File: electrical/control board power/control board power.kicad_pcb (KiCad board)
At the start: 2 copper layers, 147.3 x 147.3 mm, 80 parts, among them J1 Conn_01x02, J10 48V_from_conversion, J17 Switch_B, J18 Switch_C, J19 Switch_D, J2 5V, J3 Barrel_Jack, J4 Switch_A, J5 Switch_Input, J6 Power_Connector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

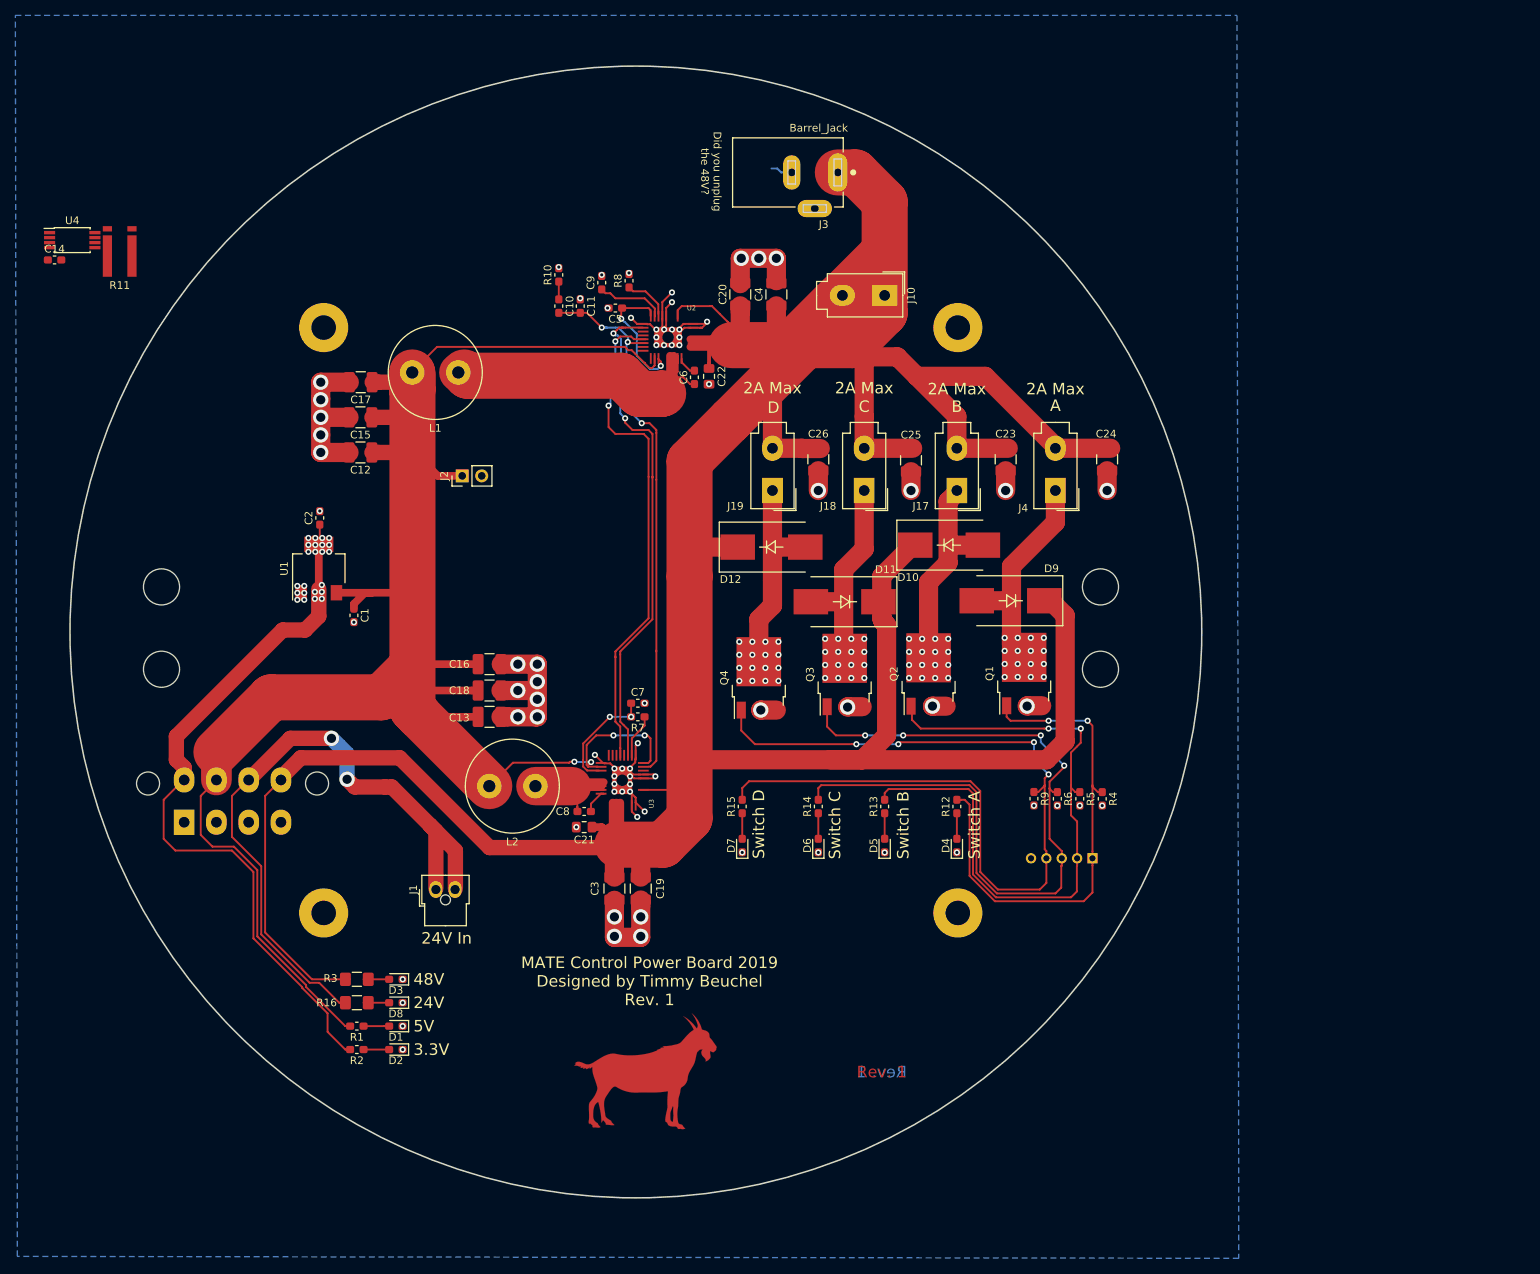
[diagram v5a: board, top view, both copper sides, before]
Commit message: Switched location of low side switches
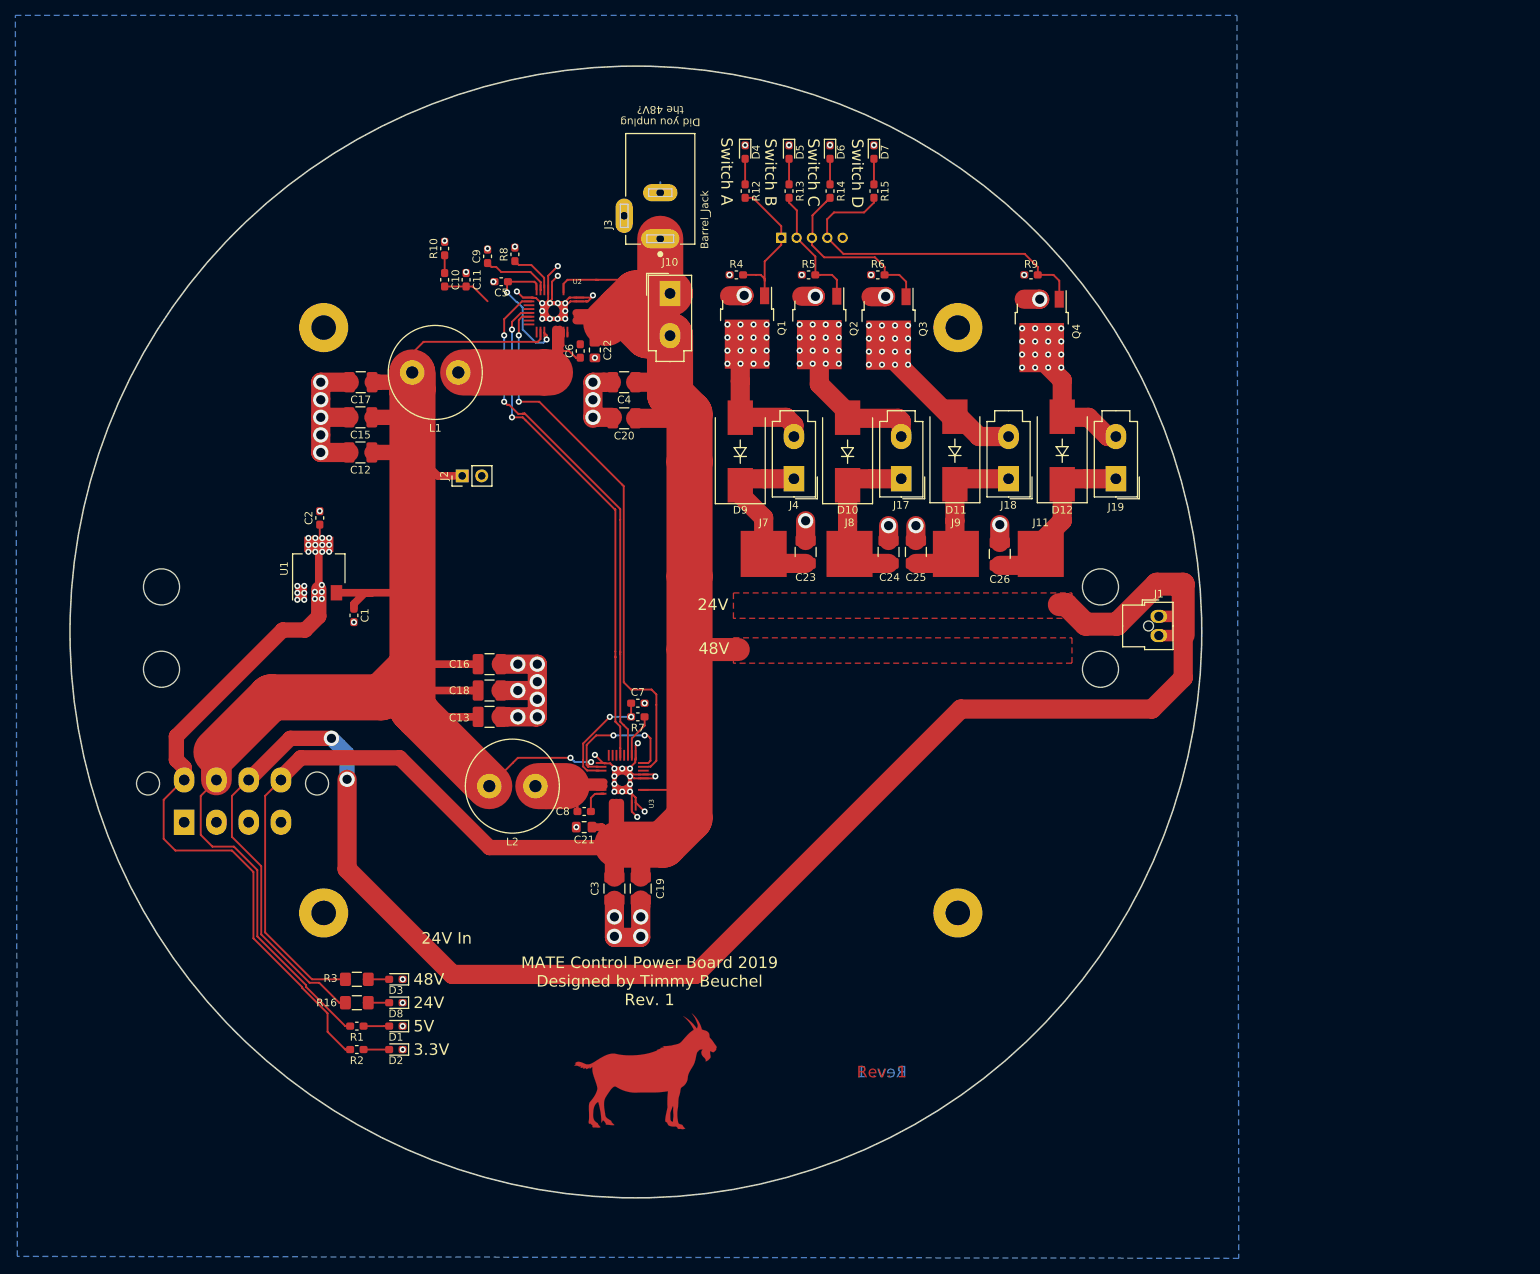
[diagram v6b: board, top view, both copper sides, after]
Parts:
- removed C14: C_Small, Capacitor_SMD:C_0603_1608Metric_Pad1.05x0.95mm_HandSolder
- removed R11: 1m, footprints:FC4L64
- removed U4: INA240-INA240, Package_SO:TSSOP-8_4.4x3mm_P0.65mm
- added J11: Switch_D_High, footprints:Square_Pad_6mm, F.Cu at (154.3, 87.6)
- added J7: Switch_A_High, footprints:Square_Pad_6mm, F.Cu at (118.2, 87.6)
- added J8: Switch_B_High, footprints:Square_Pad_6mm, F.Cu at (129.4, 87.6)
- added J9: Switch_C_High, footprints:Square_Pad_6mm, F.Cu at (143.3, 87.6)
- moved J1 100.6 mm to (169.7, 100.3), turned to 0 degrees
- moved D4 94.4 mm to (115.8, 39.9), turned to 270 degrees
- moved D7 91.9 mm to (132.6, 39.9), turned to 270 degrees
- moved D5 91.1 mm to (121.5, 39.9), turned to 270 degrees
- moved J5 90.4 mm to (120.5, 51.1), turned to 0 degrees
- moved D6 90.3 mm to (126.9, 39.9), turned to 270 degrees
- moved R12 84.7 mm to (115.8, 45.0), turned to 270 degrees
- moved R4 83.2 mm to (114.7, 55.9), turned to 180 degrees
- moved R15 81.9 mm to (132.6, 45.0), turned to 270 degrees
- moved R13 81.1 mm to (121.5, 45.0), turned to 270 degrees
- moved R14 80.1 mm to (126.9, 45.0), turned to 270 degrees
- moved R5 76.8 mm to (124.1, 55.9), turned to 180 degrees
- moved R6 72.1 mm to (133.1, 55.9), turned to 180 degrees
- moved R9 68.2 mm to (153.0, 55.9), turned to 180 degrees
- moved Q4 58.2 mm to (154.4, 63.2), turned to 270 degrees
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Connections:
- C23 pad 2: +48V -> /SWITCH_A_HIGH
- C24 pad 2: +48V -> /SWITCH_B_HIGH
- C25 pad 2: +48V -> /SWITCH_C_HIGH
- C26 pad 2: +48V -> /SWITCH_D_HIGH
- D10 pad 1: +48V -> /SWITCH_B_HIGH
- D11 pad 1: +48V -> /SWITCH_C_HIGH
- D12 pad 1: +48V -> /SWITCH_D_HIGH
- D9 pad 1: +48V -> /SWITCH_A_HIGH
- J17 pad 1: Net-(D10-Pad2) -> /SWITCH_B_HIGH
- J17 pad 2: +48V -> Net-(D10-Pad2)
- J18 pad 1: Net-(D11-Pad2) -> /SWITCH_C_HIGH
- J18 pad 2: +48V -> Net-(D11-Pad2)
- J19 pad 1: Net-(D12-Pad2) -> /SWITCH_D_HIGH
- J19 pad 2: +48V -> Net-(D12-Pad2)
- J4 pad 1: Net-(D9-Pad2) -> /SWITCH_A_HIGH
- J4 pad 2: +48V -> Net-(D9-Pad2)
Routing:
- net +48V: track 474.1 -> 240.0 mm
- net +24V: track 88.5 -> 236.9 mm
- net /SWITCH_C: track 100.0 -> 24.0 mm, vias 4 -> 0
- net /SWITCH_D: track 116.8 -> 45.6 mm, vias 4 -> 0
- net /SWITCH_B: track 86.8 -> 16.4 mm, vias 2 -> 0
- net /SWITCH_A: track 64.9 -> 19.3 mm, vias 2 -> 0
- net /SWITCH_D_HIGH: track 0.00 -> 19.6 mm
- net /SWITCH_A_HIGH: track 0.00 -> 19.6 mm
- net /SWITCH_C_HIGH: track 0.00 -> 18.6 mm
- net /SWITCH_B_HIGH: track 0.00 -> 18.3 mm
- net +5V: track 258.0 -> 241.5 mm
- net Net-(C6-Pad2): track 39.8 -> 23.3 mm
- net Net-(D12-Pad2): track 27.1 -> 15.9 mm
- net Net-(D9-Pad2): track 28.6 -> 18.8 mm
- net Net-(D10-Pad2): track 27.5 -> 19.9 mm
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- added copper zone on F.Cu, net +24V
- added copper zone on F.Cu, net +48V
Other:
- board text removed: "2A Max"
- board text removed: "A"
- board text removed: "B"
- board text removed: "C"
- board text removed: "D"

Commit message: added diode marks to diodes
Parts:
- D1, D2, D3, D4, D5, D6, D7, D8: footprint LED_SMD:LED_0603_1608Metric_Pad1.05x0.95mm_HandSolder -> footprints:LED_0603_1608Metric_Pad1.05x0.95mm_HandSolder_diode_mark
- moved R10 6.73 mm to (76.6, 59.2), turned to 180 degrees
- moved R8 5.69 mm to (91.1, 55.5), turned to 0 degrees
- moved C9 5.59 mm to (87.5, 55.5), turned to 180 degrees
- moved C10 4.60 mm to (79.6, 60.1)
- moved C11 4.60 mm to (82.4, 60.1)
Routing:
- net Net-(C9-Pad1): track 8.99 -> 3.13 mm
- net Net-(R8-Pad1): track 5.98 -> 2.25 mm
- net Net-(C6-Pad1): track 0.46 -> 3.29 mm
- net +24V: track 236.9 -> 238.9 mm
- net GND: track 127.2 -> 125.2 mm, vias 84 -> 83
- net Net-(C10-Pad2): track 77.5 -> 79.2 mm, vias 2 -> 3

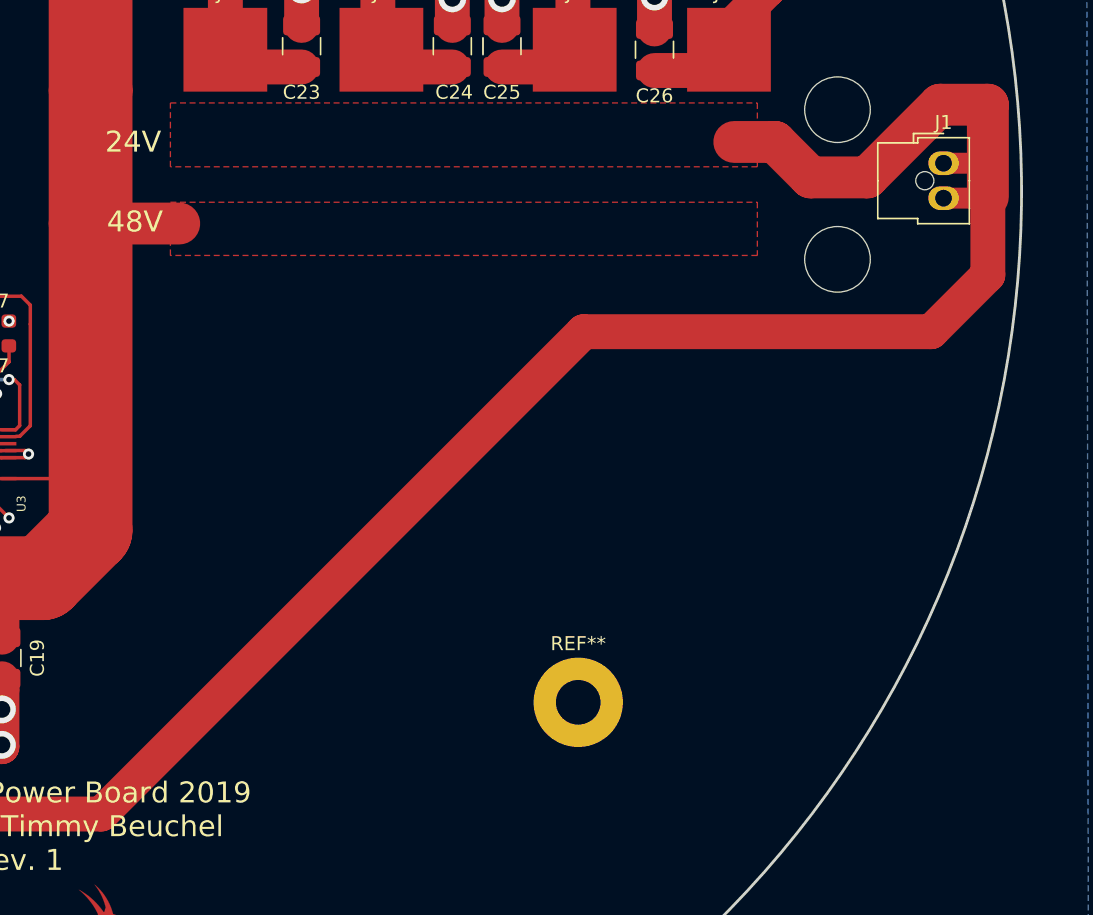
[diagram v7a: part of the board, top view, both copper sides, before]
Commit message: Removed 2 low side switches
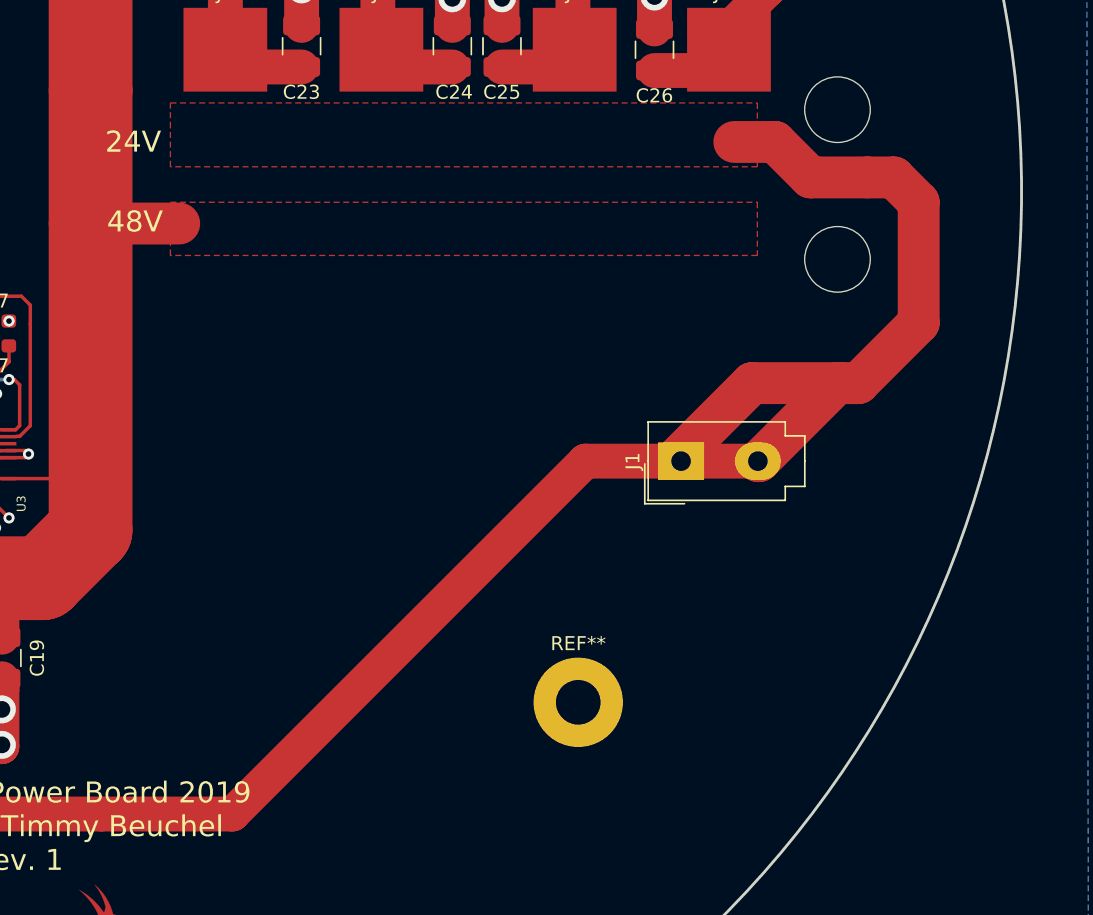
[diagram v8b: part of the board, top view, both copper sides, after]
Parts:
- J1: footprint footprints:Molex_Nano-Fit_105309-xx02_1x02_P2.50mm_Vertical_Oval_Pads -> Connector_Molex:Molex_Mini-Fit_Jr_5566-02A_2x01_P4.20mm_Vertical
- R1: value R_Small -> 330
- R12, R13, R14, R15, R2: value R_Small -> 150
- R16: value R_Small -> 2.7k
- R3: value R_Small -> 9.4k
- TB1: value Curtis_2000 -> Curtis_2010
- moved J1 28.4 mm to (150.9, 121.7), turned to 90 degrees
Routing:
- net +24V: track 238.9 -> 230.7 mm
